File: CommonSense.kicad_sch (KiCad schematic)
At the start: 29 parts, among them J1 Conn_02x04_Counter_Clockwise, U1 NRF52810-QFAA-R7, U2 SHT41-AD1B-R2, Y1 ECS-.327-12.5-12R-TR, Y2 ABM11W-32.0000MHZ-7-D1X-T3

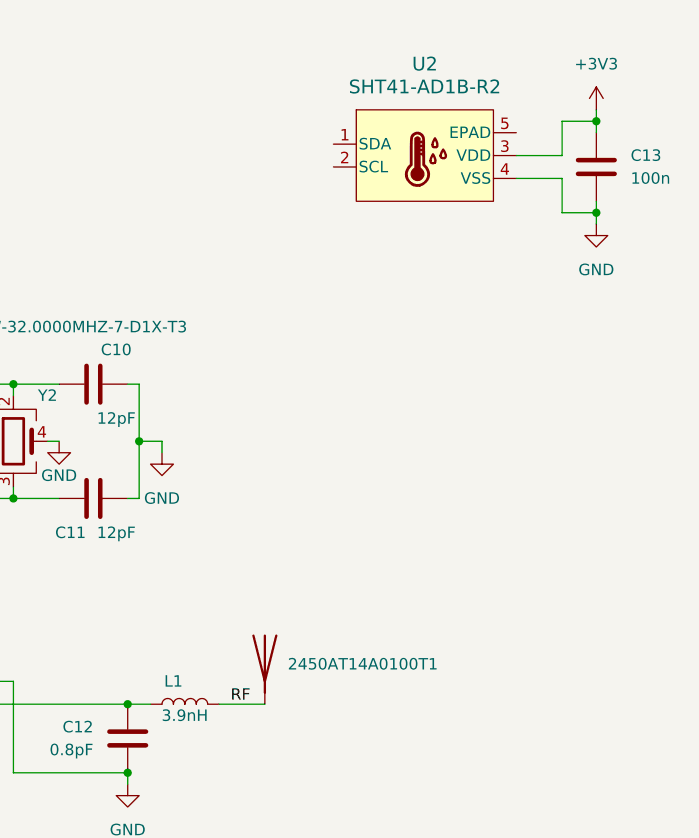
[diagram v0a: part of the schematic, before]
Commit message: Replace schematic symbols with new versions from library
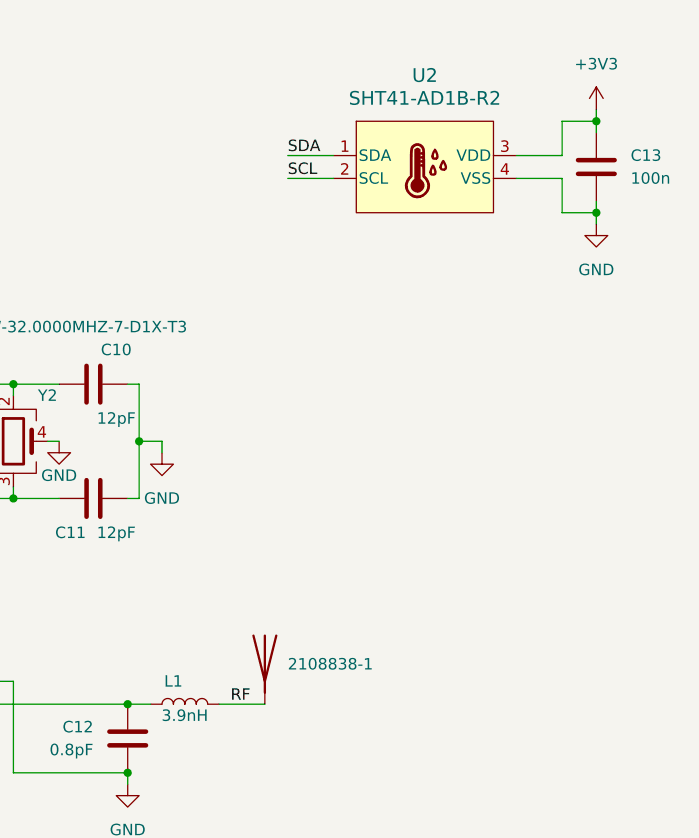
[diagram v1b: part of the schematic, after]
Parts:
- renumbered 2450AT14A0100T1 to 2108838-1
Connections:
- net SDA: now reaches U2.1 (SDA)
- net SCL: now reaches U2.2 (SCL)
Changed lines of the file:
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@@
+    (stroke (width 0) (type default))
+  )
+  (wire (pts (xy 238.76 44.45) (xy 243.84 44.45))
     (stroke (width 0) (type default))
   )
@@
   )
   (wire (pts (xy 91.44 92.71) (xy 91.44 95.25))
+    (stroke (width 0) (type default))
+  )
+  (wire (pts (xy 238.76 41.91) (xy 243.84 41.91))
     (stroke (width 0) (type default))
   )
@@
     (effects (font (size 1.27 1.27)) (justify left bottom))
   )
+  (label "SDA" (at 238.76 41.91 0) (fields_autoplaced)
+    (effects (font (size 1.27 1.27)) (justify left bottom))
+  )
   (label "SWDIO" (at 179.07 118.11 0) (fields_autoplaced)
     (effects (font (size 1.27 1.27)) (justify left bottom))
@@
   )
   (label "DEC1" (at 106.68 67.31 0) (fields_autoplaced)
+    (effects (font (size 1.27 1.27)) (justify left bottom))
+  )
+  (label "SCL" (at 238.76 44.45 0) (fields_autoplaced)
     (effects (font (size 1.27 1.27)) (justify left bottom))
   )
@@
     )
   )
-  (symbol (lib_id "encyclopedia_galactica:SHT41-AD1B-R2") (at 254 41.91 0) (unit 1)
-    (in_bom yes) (on_board yes) (dnp no) (fields_autoplaced)
-    (property "Reference" "U2" (at 254 31.75 0)
-      (effects (font (size 1.524 1.524)))
-    )
-    (property "Value" "SHT41-AD1B-R2" (at 254 34.29 0)
-      (effects (font (size 1.524 1.524)))
-    )
-    (property "Footprint" "encyclopedia_galactica:DFN4_SHT41_SEN" (at 254 20.32 0)
-      (effects (font (size 1.27 1.27) italic) hide)
-    )
-    (property "Datasheet" "https://sensirion.com/media/documents/33FD6951/63E1087C/Datasheet_SHT4x_1.pdf" (at 254 17.78 0)
-      (effects (font (size 1.27 1.27) italic) hide)
-    )
-    (pin "1")
-    (pin "2")
-    (pin "3")
-    (pin "4")
-    (pin "5")
-    (instances
-      (project "CommonSense"
-        (path "/38fbf0b5-ae68-401e-b1a9-e916ed01fc13"
-          (reference "U2") (unit 1)
-        )
-      )
-    )
-  )
   (symbol (lib_id "Device:C") (at 273.05 43.18 0) (unit 1)
     (in_bom yes) (on_board yes) (dnp no)
@@
         (path "/523ef776-806b-43b6-937c-22b5e6ba7731"
           (reference "Y1") (unit 1)
+        )
+      )
+    )
+  )
+  (symbol (lib_id "encyclopedia_galactica:SHT41-AD1B-R2") (at 254 43.18 0) (unit 1)
+    (in_bom yes) (on_board yes) (dnp no) (fields_autoplaced)
+    (property "Reference" "U2" (at 254 33.02 0)
+      (effects (font (size 1.524 1.524)))
+    )
+    (property "Value" "SHT41-AD1B-R2" (at 254 35.56 0)
+      (effects (font (size 1.524 1.524)))
+    )
+    (property "Footprint" "encyclopedia_galactica:DFN4_SHT41_SEN" (at 254 21.59 0)
+      (effects (font (size 1.27 1.27) italic) hide)
+    )
+    (property "Datasheet" "https://sensirion.com/media/documents/33FD6951/63E1087C/Datasheet_SHT4x_1.pdf" (at 254 19.05 0)
+      (effects (font (size 1.27 1.27) italic) hide)
+    )
+    (pin "1")
+    (pin "2")
+    (pin "3")
+    (pin "4")
+    (instances
+      (project "CommonSense"
+        (path "/38fbf0b5-ae68-401e-b1a9-e916ed01fc13"
+          (reference "U2") (unit 1)
         )
       )
@@
   (symbol (lib_id "Device:Antenna") (at 236.22 97.79 0) (unit 1)
     (in_bom yes) (on_board yes) (dnp no) (fields_autoplaced)
-    (property "Reference" "2450AT14A0100T1" (at 238.76 98.425 0)
+    (property "Reference" "2108838-1" (at 238.76 98.425 0)
       (effects (font (size 1.27 1.27)) (justify left))
     )
@@
       (project "CommonSense"
         (path "/38fbf0b5-ae68-401e-b1a9-e916ed01fc13"
-          (reference "2450AT14A0100T1") (unit 1)
-        )
-      )
+          (reference "2108838-1") (unit 1)
+        )
+      )

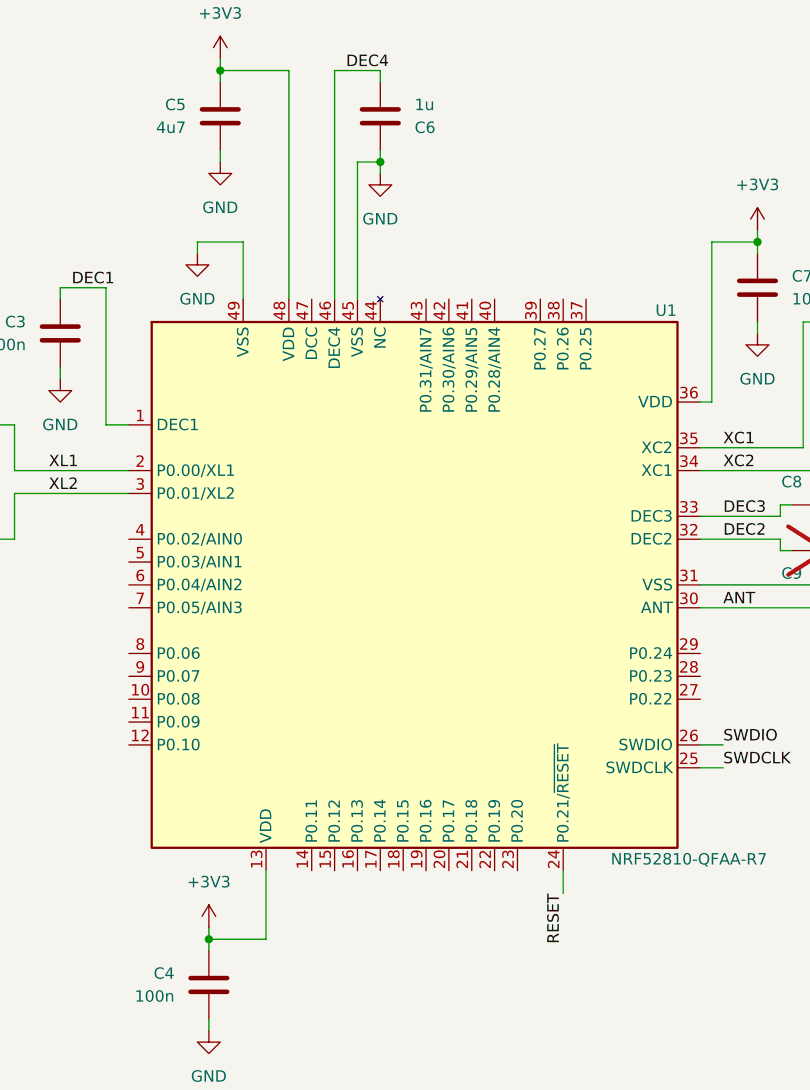
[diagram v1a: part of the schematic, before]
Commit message: Fix most DRC violations
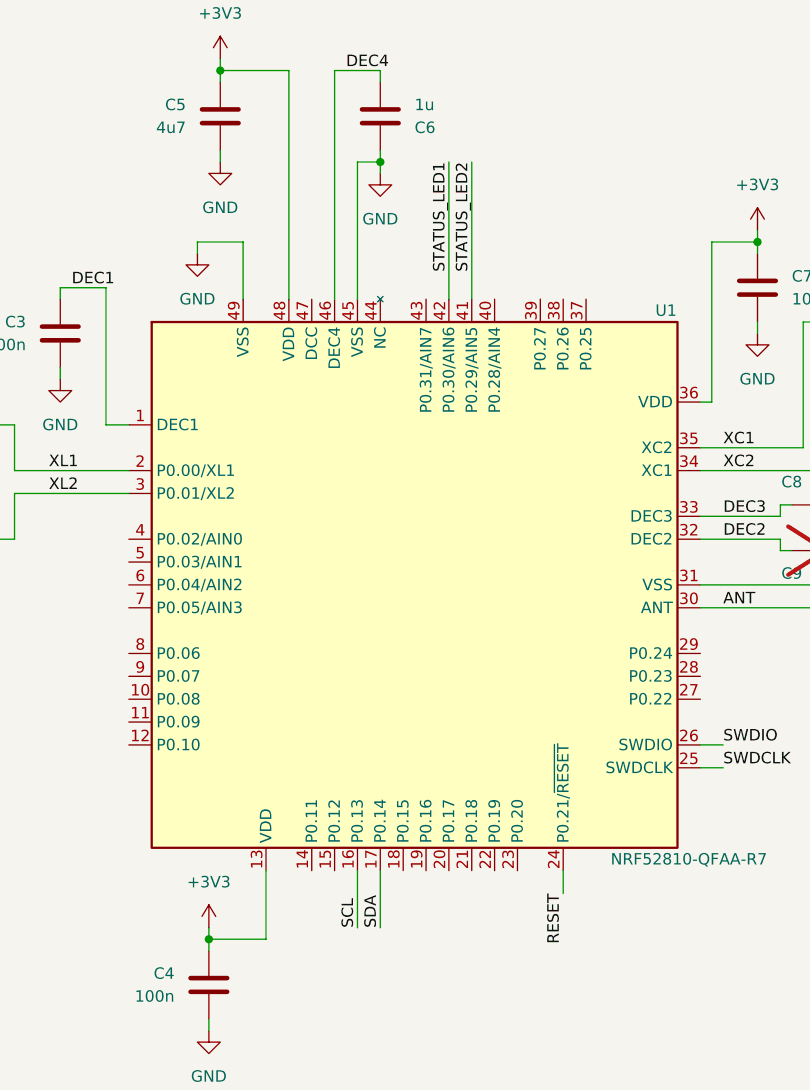
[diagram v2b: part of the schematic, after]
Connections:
- net SCL: now also U1.16 (P0.13)
- net SDA: now also U1.17 (P0.14)
- net STATUS_LED1: now also U1.42 (P0.30/AIN6)
- net STATUS_LED2: now also U1.41 (P0.29/AIN5)
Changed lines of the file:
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@@
+    (stroke (width 0) (type default))
+  )
+  (wire (pts (xy 138.43 132.08) (xy 138.43 138.43))
     (stroke (width 0) (type default))
   )
@@
     (stroke (width 0) (type default))
   )
+  (wire (pts (xy 148.59 53.34) (xy 148.59 68.58))
+    (stroke (width 0) (type default))
+  )
   (wire (pts (xy 269.24 38.1) (xy 273.05 38.1))
     (stroke (width 0) (type default))
@@
     (stroke (width 0) (type default))
   )
+  (wire (pts (xy 151.13 53.34) (xy 151.13 68.58))
+    (stroke (width 0) (type default))
+  )
   (wire (pts (xy 44.45 77.47) (xy 44.45 80.01))
     (stroke (width 0) (type default))
@@
   )
   (wire (pts (xy 269.24 41.91) (xy 269.24 38.1))
+    (stroke (width 0) (type default))
+  )
+  (wire (pts (xy 140.97 132.08) (xy 140.97 138.43))
     (stroke (width 0) (type default))
   )
@@
     (effects (font (size 1.27 1.27)) (justify right bottom))
   )
+  (label "SCL" (at 138.43 138.43 90) (fields_autoplaced)
+    (effects (font (size 1.27 1.27)) (justify left bottom))
+  )
   (label "DEC3" (at 179.07 92.71 0) (fields_autoplaced)
     (effects (font (size 1.27 1.27)) (justify left bottom))
@@
   (label "RF" (at 232.41 102.87 0) (fields_autoplaced)
     (effects (font (size 1.27 1.27)) (justify left bottom))
+  )
+  (label "STATUS_LED2" (at 151.13 53.34 270) (fields_autoplaced)
+    (effects (font (size 1.27 1.27)) (justify right bottom))
   )
   (label "XL2" (at 104.14 90.17 0) (fields_autoplaced)
@@
     (effects (font (size 1.27 1.27)) (justify left bottom))
   )
+  (label "SDA" (at 140.97 138.43 90) (fields_autoplaced)
+    (effects (font (size 1.27 1.27)) (justify left bottom))
+  )
   (label "SCL" (at 238.76 44.45 0) (fields_autoplaced)
     (effects (font (size 1.27 1.27)) (justify left bottom))
@@
     (effects (font (size 1.27 1.27)) (justify left bottom))
   )
+  (label "STATUS_LED1" (at 148.59 53.34 270) (fields_autoplaced)
+    (effects (font (size 1.27 1.27)) (justify right bottom))
+  )
   (label "DEC4" (at 137.16 43.18 0) (fields_autoplaced)

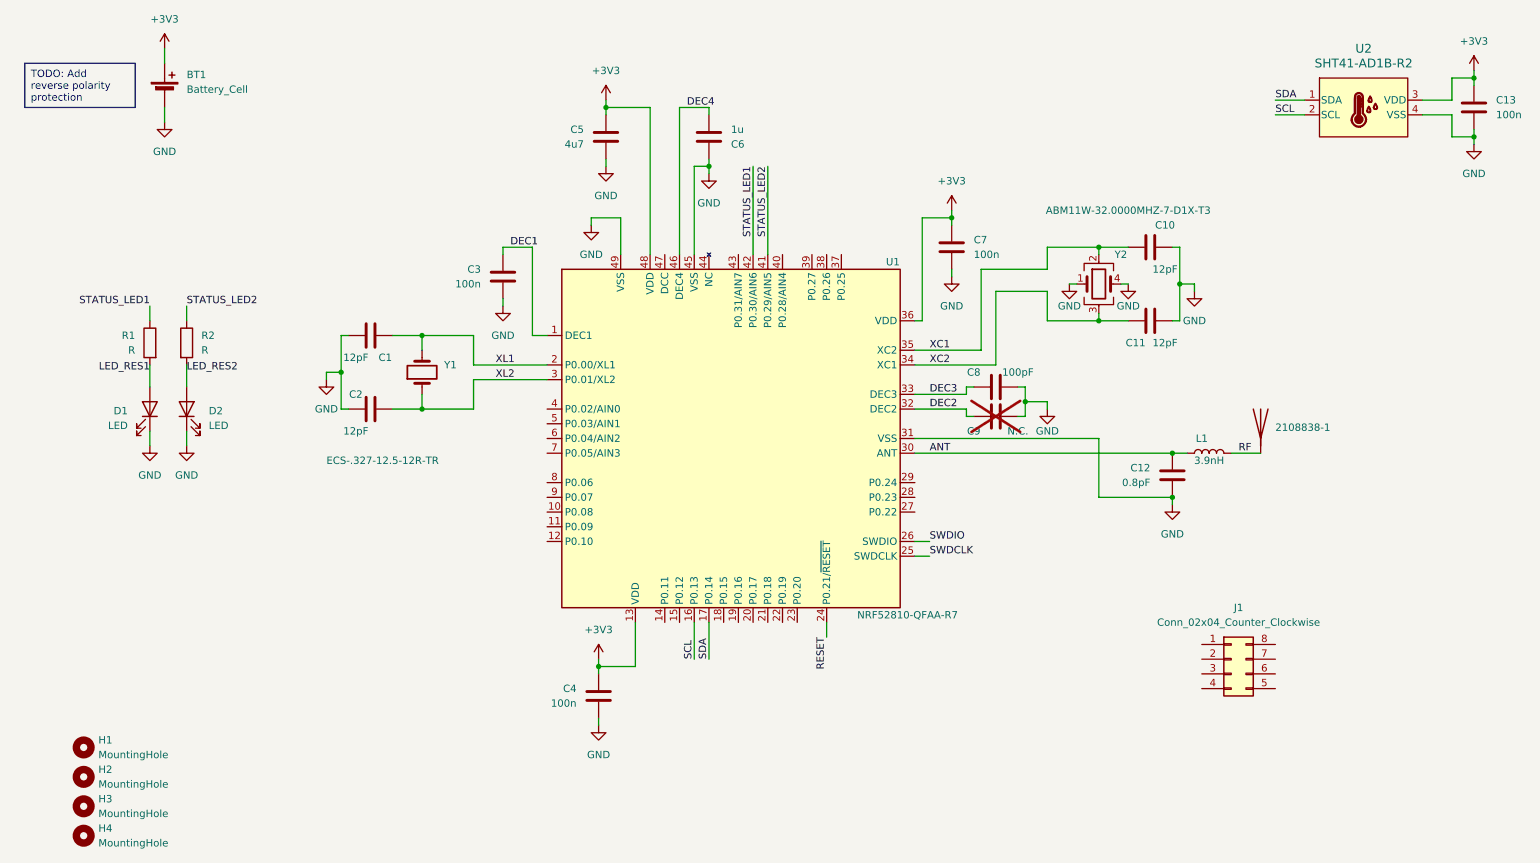
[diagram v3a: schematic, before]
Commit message: Tidy up schematic and add I2C pullup resistors
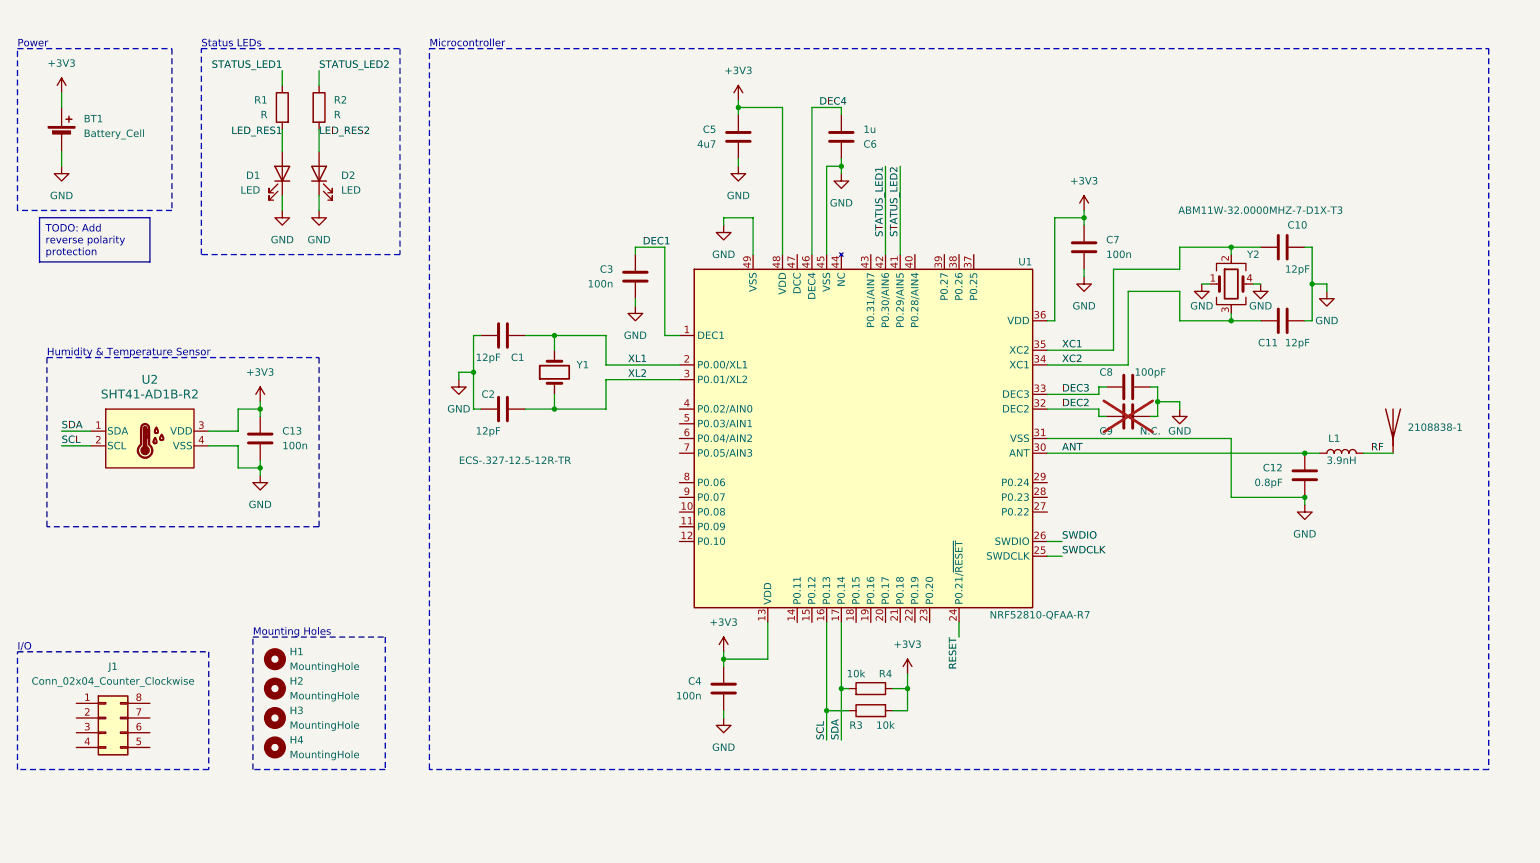
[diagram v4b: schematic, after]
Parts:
- added R3, R4: 10k, symbol Device:R
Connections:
- net +3V3: now also R3.2, R4.1
- net SCL: now also R3.1
- net SDA: now also R4.2
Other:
- note added: "Humidity & Temperature Sensor"
- note added: "I/O"
- note added: "Microcontroller"
- note added: "Mounting Holes"
- note added: "Power"
- note added: "Status LEDs"
- moved on the sheet: 2108838-1, BT1, C1, C10, C11, C12, C13, C2, C3, C4, C5, C6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

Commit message: Add I2C pullup resistors to PCB
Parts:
- R3, R4: footprint (none) -> Resistor_SMD:R_0603_1608Metric
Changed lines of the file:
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@@
       (effects (font (size 1.27 1.27)))
     )
-    (property "Footprint" "" (at 168.91 145.542 90)
+    (property "Footprint" "Resistor_SMD:R_0603_1608Metric" (at 168.91 145.542 90)
       (effects (font (size 1.27 1.27)) hide)
     )
@@
       (effects (font (size 1.27 1.27)))
     )
-    (property "Footprint" "" (at 168.91 145.288 90)
-      (effects (font (size 1.27 1.27)) hide)
-    )
+    (property "Footprint" "Resistor_SMD:R_0603_1608Metric" (at 168.91 145.288 90)
+      (effects (font (size 1.27 1.27)) hide)
+    )
